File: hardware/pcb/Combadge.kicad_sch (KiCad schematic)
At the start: 19 parts, among them J1 Conn_01x02_Female, J2 Conn_01x02_Female, J3 TOUCH, U1 ESP32-WROOM-32, U2 MAX98357AEWL+T

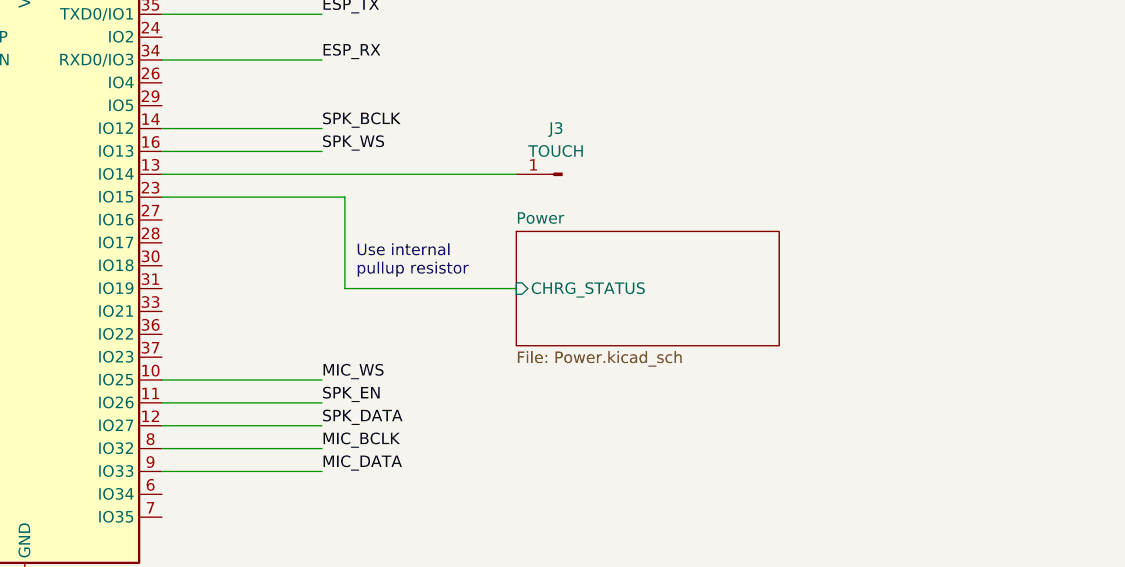
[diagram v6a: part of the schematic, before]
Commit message: Add indicator LED
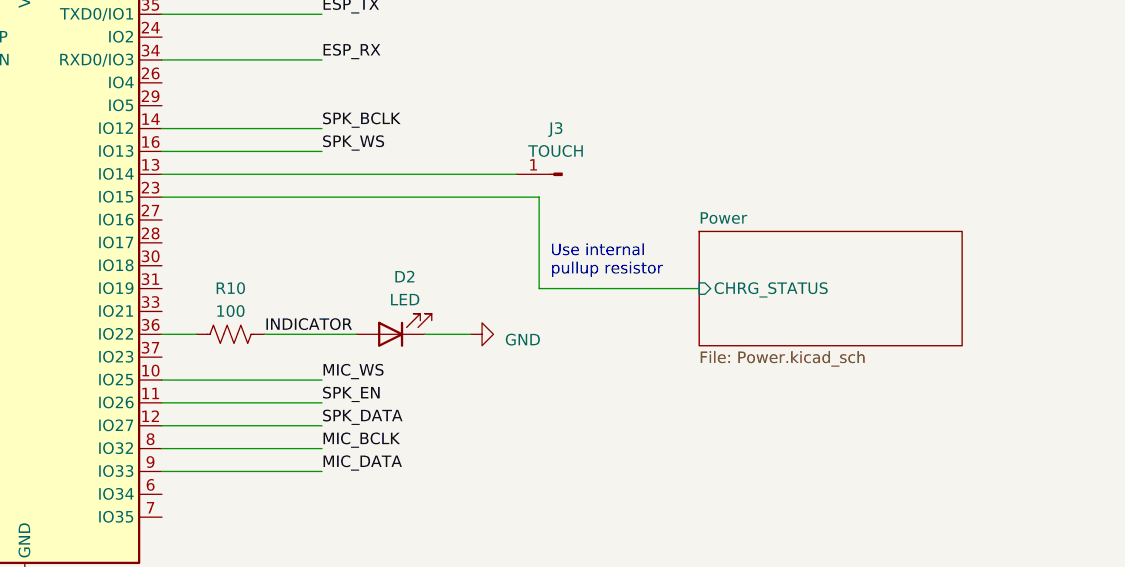
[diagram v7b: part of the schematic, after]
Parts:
- added D2: LED, LED_SMD:LED_1206_3216Metric_Pad1.42x1.75mm_HandSolder, symbol Device:LED
- added R10: 100, Resistor_SMD:R_1206_3216Metric_Pad1.30x1.75mm_HandSolder, symbol Device:R_US
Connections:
- net GND: now also D2.1 (K)
- net at U1.36 (IO22): now also R10.1
- new net INDICATOR: D2.2 (A), R10.2
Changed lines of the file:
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@@
+    (stroke (width 0) (type default))
+  )
+  (wire (pts (xy 88.9 93.98) (xy 92.71 93.98))
     (stroke (width 0) (type default))
   )
@@
     (stroke (width 0) (type default))
   )
-  (wire (pts (xy 109.22 88.9) (xy 128.27 88.9))
+  (wire (pts (xy 130.81 88.9) (xy 148.59 88.9))
     (stroke (width 0) (type default))
   )
@@
     (stroke (width 0) (type default))
   )
-  (wire (pts (xy 109.22 78.74) (xy 109.22 88.9))
+  (wire (pts (xy 130.81 78.74) (xy 130.81 88.9))
     (stroke (width 0) (type default))
   )
@@
     (stroke (width 0) (type default))
   )
+  (wire (pts (xy 100.33 93.98) (xy 110.49 93.98))
+    (stroke (width 0) (type default))
+  )
   (wire (pts (xy 250.19 151.13) (xy 257.81 151.13))
     (stroke (width 0) (type default))
@@
     (stroke (width 0) (type default))
   )
-  (wire (pts (xy 88.9 78.74) (xy 109.22 78.74))
+  (wire (pts (xy 88.9 78.74) (xy 130.81 78.74))
     (stroke (width 0) (type default))
   )
@@
     (stroke (width 0) (type default))
   )
+  (wire (pts (xy 118.11 93.98) (xy 123.19 93.98))
+    (stroke (width 0) (type default))
+  )
   (wire (pts (xy 146.05 143.51) (xy 148.59 143.51))
     (stroke (width 0) (type default))
@@
     (stroke (width 0) (type default))
   )
-  (text "Use internal\npullup resistor" (at 110.49 87.63 0)
+  (text "Use internal\npullup resistor" (at 132.08 87.63 0)
     (effects (font (size 1.27 1.27)) (justify left bottom))
   )
@@
     (effects (font (size 1.27 1.27)) (justify left bottom))
   )
+  (label "INDICATOR" (at 100.33 93.98 0) (fields_autoplaced)
+    (effects (font (size 1.27 1.27)) (justify left bottom))
+  )
   (label "SPK-" (at 224.79 114.3 0) (fields_autoplaced)
     (effects (font (size 1.27 1.27)) (justify left bottom))
@@
         (path "/dc42e7bc-f663-434d-8744-232038ac4fdf"
           (reference "#PWR02") (unit 1)
+        )
+      )
+    )
+  )
+  (symbol (lib_id "Device:R_US") (at 96.52 93.98 90) (unit 1)
+    (in_bom yes) (on_board yes) (dnp no) (fields_autoplaced)
+    (property "Reference" "R10" (at 96.52 88.9 90)
+      (effects (font (size 1.27 1.27)))
+    )
+    (property "Value" "100" (at 96.52 91.44 90)
+      (effects (font (size 1.27 1.27)))
+    )
+    (property "Footprint" "Resistor_SMD:R_1206_3216Metric_Pad1.30x1.75mm_HandSolder" (at 96.774 92.964 90)
+      (effects (font (size 1.27 1.27)) hide)
+    )
+    (property "Datasheet" "~" (at 96.52 93.98 0)
+      (effects (font (size 1.27 1.27)) hide)
+    )
+    (pin "1")
+    (pin "2")
+    (instances
+      (project "Combadge"
+        (path "/dc42e7bc-f663-434d-8744-232038ac4fdf"
+          (reference "R10") (unit 1)
         )
       )
@@
     )
   )
+  (symbol (lib_name "GND_1") (lib_id "power:GND") (at 123.19 93.98 90) (unit 1)
+    (in_bom yes) (on_board yes) (dnp no) (fields_autoplaced)
+    (property "Reference" "#PWR020" (at 129.54 93.98 0)
+      (effects (font (size 1.27 1.27)) hide)
+    )
+    (property "Value" "GND" (at 127 94.615 90)
+      (effects (font (size 1.27 1.27)) (justify right))
+    )
+    (property "Footprint" "" (at 123.19 93.98 0)
+      (effects (font (size 1.27 1.27)) hide)
+    )
+    (property "Datasheet" "" (at 123.19 93.98 0)
+      (effects (font (size 1.27 1.27)) hide)
+    )
+    (pin "1")
+    (instances
+      (project "Combadge"
+        (path "/dc42e7bc-f663-434d-8744-232038ac4fdf"
+          (reference "#PWR020") (unit 1)
+        )
+      )
+    )
+  )
   (symbol (lib_id "Connector:Conn_01x02_Female") (at 39.37 176.53 0) (unit 1)
     (in_bom yes) (on_board yes) (dnp no) (fields_autoplaced)
@@
     )
   )
+  (symbol (lib_id "Device:LED") (at 114.3 93.98 180) (unit 1)
+    (in_bom yes) (on_board yes) (dnp no) (fields_autoplaced)
+    (property "Reference" "D2" (at 115.8875 87.63 0)
+      (effects (font (size 1.27 1.27)))
+    )
+    (property "Value" "LED" (at 115.8875 90.17 0)
+      (effects (font (size 1.27 1.27)))
+    )
+    (property "Footprint" "LED_SMD:LED_1206_3216Metric_Pad1.42x1.75mm_HandSolder" (at 114.3 93.98 0)
+      (effects (font (size 1.27 1.27)) hide)
+    )
+    (property "Datasheet" "~" (at 114.3 93.98 0)
+      (effects (font (size 1.27 1.27)) hide)
+    )
+    (pin "1")
+    (pin "2")
+    (instances
+      (project "Combadge"
+        (path "/dc42e7bc-f663-434d-8744-232038ac4fdf"
+          (reference "D2") (unit 1)
+        )
+      )
+    )
+  )
   (symbol (lib_id "power:+3.3V") (at 205.74 34.29 90) (unit 1)
     (in_bom yes) (on_board yes) (dnp no) (fields_autoplaced)
@@
     )
   )
-  (sheet (at 128.27 82.55) (size 29.21 12.7) (fields_autoplaced)
+  (sheet (at 148.59 82.55) (size 29.21 12.7) (fields_autoplaced)
     (stroke (width 0.1524) (type solid))
     (fill (color 0 0 0 0.0000))
-    (property "Sheetname" "Power" (at 128.27 81.8384 0)
+    (property "Sheetname" "Power" (at 148.59 81.8384 0)
       (effects (font (size 1.27 1.27)) (justify left bottom))
     )
-    (property "Sheetfile" "Power.kicad_sch" (at 128.27 95.8346 0)
+    (property "Sheetfile" "Power.kicad_sch" (at 148.59 95.8346 0)
       (effects (font (size 1.27 1.27)) (justify left top))
     )
-    (pin "CHRG_STATUS" input (at 128.27 88.9 180)
-      (effects (font (size 1.27 1.27)) (justify left))
-    )
+    (pin "CHRG_STATUS" input (at 148.59 88.9 180)
+      (effects (font (size 1.27 1.27)) (justify left))
+    )

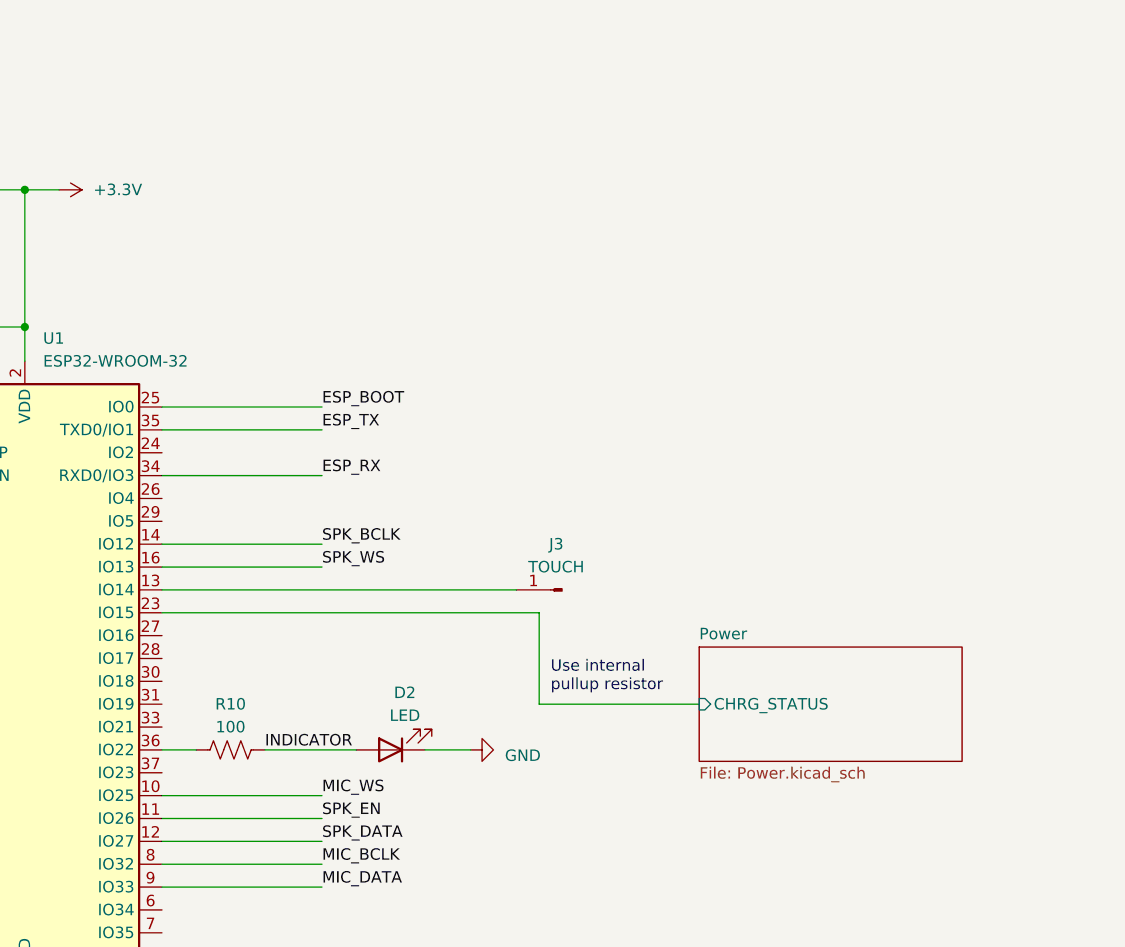
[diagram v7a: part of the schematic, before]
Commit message: Replace zener diode setup with TLV431
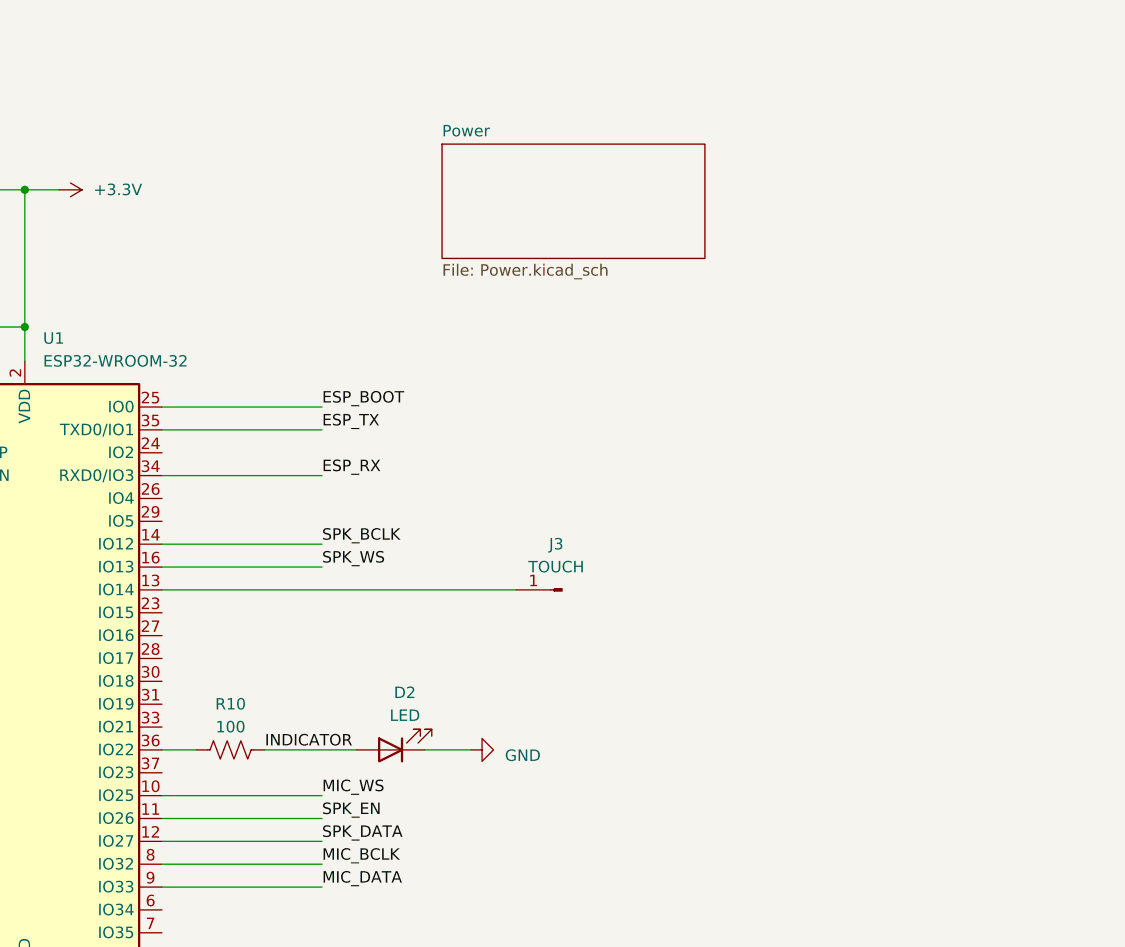
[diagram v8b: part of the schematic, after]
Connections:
- net Power/CHRG_STATUS: no longer names the net of U1.23 (IO15)
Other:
- sheet Power ports: added none; removed CHRG_STATUS
- note removed: "Use internal pullup resistor"
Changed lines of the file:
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@@
-    (stroke (width 0) (type default))
-  )
-  (wire (pts (xy 130.81 88.9) (xy 148.59 88.9))
     (stroke (width 0) (type default))
   )
@@
     (stroke (width 0) (type default))
   )
-  (wire (pts (xy 130.81 78.74) (xy 130.81 88.9))
-    (stroke (width 0) (type default))
-  )
   (wire (pts (xy 152.4 158.75) (xy 148.59 158.75))
     (stroke (width 0) (type default))
@@
     (stroke (width 0) (type default))
   )
-  (wire (pts (xy 88.9 78.74) (xy 130.81 78.74))
-    (stroke (width 0) (type default))
-  )
   (wire (pts (xy 36.83 36.83) (xy 44.45 36.83))
     (stroke (width 0) (type default))
@@
   (wire (pts (xy 251.46 27.94) (xy 251.46 29.21))
     (stroke (width 0) (type default))
-  )
-  (text "Use internal\npullup resistor" (at 132.08 87.63 0)
-    (effects (font (size 1.27 1.27)) (justify left bottom))
   )
   (text "Makes IC respond\nto right WS signal" (at 179.07 133.35 0)
@@
     )
   )
-  (sheet (at 148.59 82.55) (size 29.21 12.7) (fields_autoplaced)
+  (sheet (at 120.015 26.67) (size 29.21 12.7) (fields_autoplaced)
     (stroke (width 0.1524) (type solid))
     (fill (color 0 0 0 0.0000))
-    (property "Sheetname" "Power" (at 148.59 81.8384 0)
+    (property "Sheetname" "Power" (at 120.015 25.9584 0)
       (effects (font (size 1.27 1.27)) (justify left bottom))
     )
-    (property "Sheetfile" "Power.kicad_sch" (at 148.59 95.8346 0)
+    (property "Sheetfile" "Power.kicad_sch" (at 120.015 39.9546 0)
       (effects (font (size 1.27 1.27)) (justify left top))
     )
-    (pin "CHRG_STATUS" input (at 148.59 88.9 180)
-      (effects (font (size 1.27 1.27)) (justify left))
-    )
-    (instances
+    (instances
